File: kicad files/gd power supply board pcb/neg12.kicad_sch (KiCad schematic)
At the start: 22 parts, among them U1 MAX17580

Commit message: before erc
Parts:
- added H1, H2, H3, H4: MountingHole, MountingHole:MountingHole_2.2mm_M2, symbol Mechanical:MountingHole
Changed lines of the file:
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@@
     (effects (font (size 1.27 1.27)) (justify right))
+  )
+  (symbol (lib_id "Mechanical:MountingHole") (at 195.58 50.8 0) (unit 1)
+    (in_bom yes) (on_board yes) (fields_autoplaced)
+    (property "Reference" "H1" (id 0) (at 198.12 49.5299 0)
+      (effects (font (size 1.27 1.27)) (justify left))
+    )
+    (property "Value" "MountingHole" (id 1) (at 198.12 52.0699 0)
+      (effects (font (size 1.27 1.27)) (justify left))
+    )
+    (property "Footprint" "MountingHole:MountingHole_2.2mm_M2" (id 2) (at 195.58 50.8 0)
+      (effects (font (size 1.27 1.27)) hide)
+    )
+    (property "Datasheet" "~" (id 3) (at 195.58 50.8 0)
+      (effects (font (size 1.27 1.27)) hide)
+    )
   )
   (symbol (lib_id "My Library:TestPoint_Harwin") (at 146.05 74.93 0) (unit 1)
@@
     (pin "2")
   )
+  (symbol (lib_id "Mechanical:MountingHole") (at 195.58 57.15 0) (unit 1)
+    (in_bom yes) (on_board yes) (fields_autoplaced)
+    (property "Reference" "H2" (id 0) (at 198.12 55.8799 0)
+      (effects (font (size 1.27 1.27)) (justify left))
+    )
+    (property "Value" "MountingHole" (id 1) (at 198.12 58.4199 0)
+      (effects (font (size 1.27 1.27)) (justify left))
+    )
+    (property "Footprint" "MountingHole:MountingHole_2.2mm_M2" (id 2) (at 195.58 57.15 0)
+      (effects (font (size 1.27 1.27)) hide)
+    )
+    (property "Datasheet" "~" (id 3) (at 195.58 57.15 0)
+      (effects (font (size 1.27 1.27)) hide)
+    )
+  )
   (symbol (lib_id "power:GND") (at 198.12 88.9 0) (unit 1)
     (in_bom yes) (on_board yes) (fields_autoplaced)
@@
     (pin "2")
   )
+  (symbol (lib_id "Mechanical:MountingHole") (at 204.47 57.15 0) (unit 1)
+    (in_bom yes) (on_board yes) (fields_autoplaced)
+    (property "Reference" "H4" (id 0) (at 207.01 55.8799 0)
+      (effects (font (size 1.27 1.27)) (justify left))
+    )
+    (property "Value" "MountingHole" (id 1) (at 207.01 58.4199 0)
+      (effects (font (size 1.27 1.27)) (justify left))
+    )
+    (property "Footprint" "MountingHole:MountingHole_2.2mm_M2" (id 2) (at 204.47 57.15 0)
+      (effects (font (size 1.27 1.27)) hide)
+    )
+    (property "Datasheet" "~" (id 3) (at 204.47 57.15 0)
+      (effects (font (size 1.27 1.27)) hide)
+    )
+  )
   (symbol (lib_id "My Library:TestPoint_Harwin") (at 102.87 74.93 0) (unit 1)
     (in_bom yes) (on_board yes)
@@
     (pin "1")
   )
+  (symbol (lib_id "Mechanical:MountingHole") (at 204.47 50.8 0) (unit 1)
+    (in_bom yes) (on_board yes) (fields_autoplaced)
+    (property "Reference" "H3" (id 0) (at 207.01 49.5299 0)
+      (effects (font (size 1.27 1.27)) (justify left))
+    )
+    (property "Value" "MountingHole" (id 1) (at 207.01 52.0699 0)
+      (effects (font (size 1.27 1.27)) (justify left))
+    )
+    (property "Footprint" "MountingHole:MountingHole_2.2mm_M2" (id 2) (at 204.47 50.8 0)
+      (effects (font (size 1.27 1.27)) hide)
+    )
+    (property "Datasheet" "~" (id 3) (at 204.47 50.8 0)
+      (effects (font (size 1.27 1.27)) hide)
+    )
+  )
   (symbol (lib_id "My Library:R_0805") (at 151.13 74.93 90) (unit 1)

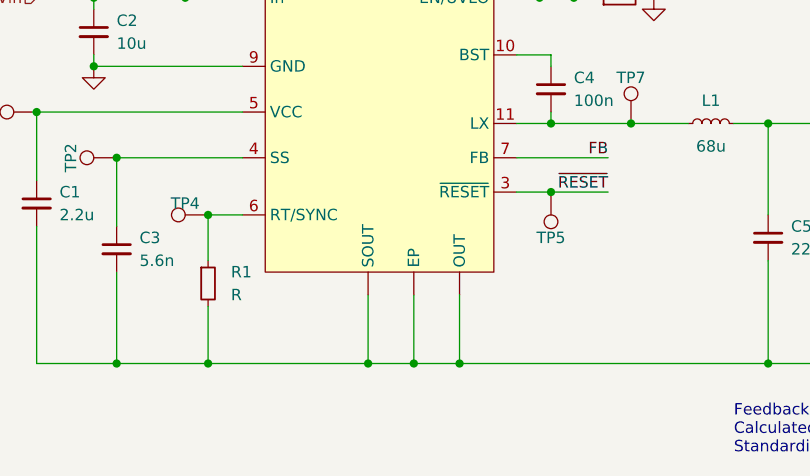
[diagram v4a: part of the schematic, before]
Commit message: initial floor planning done
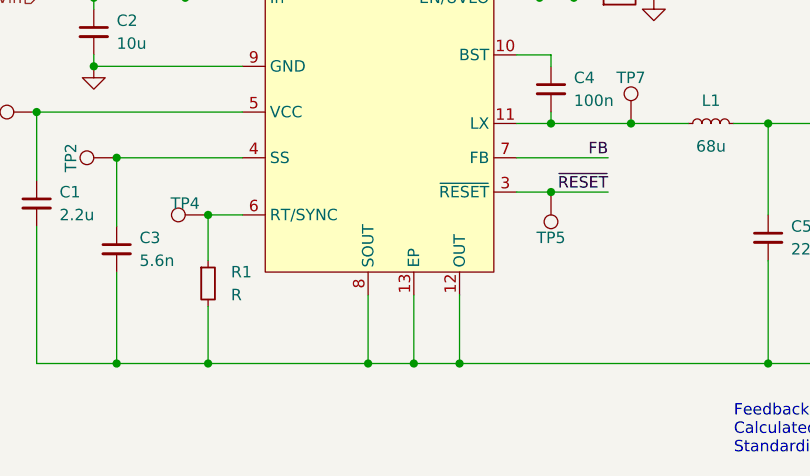
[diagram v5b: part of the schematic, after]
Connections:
- net Neg12_Out: now also U1.12 (OUT), U1.13 (EP), U1.8 (SOUT); no longer U1. (SOUT)
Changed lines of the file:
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@@
   (junction (at 102.87 74.93) (diameter 0) (color 0 0 0 0)
   )
+  (junction (at 105.41 115.57) (diameter 0) (color 0 0 0 0)
+  )
+  (junction (at 128.27 115.57) (diameter 0) (color 0 0 0 0)
+  )
+  (junction (at 86.36 87.63) (diameter 0) (color 0 0 0 0)
+  )
+  (junction (at 95.25 92.71) (diameter 0) (color 0 0 0 0)
+  )
+  (junction (at 179.07 115.57) (diameter 0) (color 0 0 0 0)
+  )
+  (junction (at 179.07 88.9) (diameter 0) (color 0 0 0 0)
+  )
+  (junction (at 143.51 88.9) (diameter 0) (color 0 0 0 0)
+  )
+  (junction (at 189.23 115.57) (diameter 0) (color 0 0 0 0)
+  )
+  (junction (at 167.64 88.9) (diameter 0) (color 0 0 0 0)
+  )
   (junction (at 123.19 115.57) (diameter 0) (color 0 0 0 0)
   )
-  (junction (at 105.41 115.57) (diameter 0) (color 0 0 0 0)
-  )
-  (junction (at 128.27 115.57) (diameter 0) (color 0 0 0 0)
-  )
-  (junction (at 86.36 87.63) (diameter 0) (color 0 0 0 0)
-  )
-  (junction (at 95.25 92.71) (diameter 0) (color 0 0 0 0)
-  )
-  (junction (at 179.07 115.57) (diameter 0) (color 0 0 0 0)
-  )
-  (junction (at 179.07 88.9) (diameter 0) (color 0 0 0 0)
-  )
-  (junction (at 143.51 88.9) (diameter 0) (color 0 0 0 0)
-  )
-  (junction (at 189.23 115.57) (diameter 0) (color 0 0 0 0)
-  )
-  (junction (at 167.64 88.9) (diameter 0) (color 0 0 0 0)
-  )
   (junction (at 143.51 96.52) (diameter 0) (color 0 0 0 0)
   )
@@
     (stroke (width 0) (type default) (color 0 0 0 0))
   )
+  (wire (pts (xy 123.19 107.95) (xy 123.19 115.57))
+    (stroke (width 0) (type default) (color 0 0 0 0))
+  )
   (wire (pts (xy 92.71 74.93) (xy 86.36 74.93))
     (stroke (width 0) (type default) (color 0 0 0 0))
@@
     (stroke (width 0) (type default) (color 0 0 0 0))
   )
+  (wire (pts (xy 123.19 115.57) (xy 128.27 115.57))
+    (stroke (width 0) (type default) (color 0 0 0 0))
+  )
   (wire (pts (xy 95.25 115.57) (xy 105.41 115.57))
     (stroke (width 0) (type default) (color 0 0 0 0))
@@
     (stroke (width 0) (type default) (color 0 0 0 0))
   )
-  (wire (pts (xy 123.19 115.57) (xy 128.27 115.57))
-    (stroke (width 0) (type default) (color 0 0 0 0))
-  )
   (wire (pts (xy 86.36 100.33) (xy 86.36 115.57))
-    (stroke (width 0) (type default) (color 0 0 0 0))
-  )
-  (wire (pts (xy 123.19 107.95) (xy 123.19 115.57))
     (stroke (width 0) (type default) (color 0 0 0 0))
   )
@@
       (effects (font (size 1.27 1.27)) hide)
     )
-    (pin "")
-    (pin "")
-    (pin "")
+    (pin "13")
+    (pin "12")
+    (pin "8")
     (pin "1")
     (pin "10")

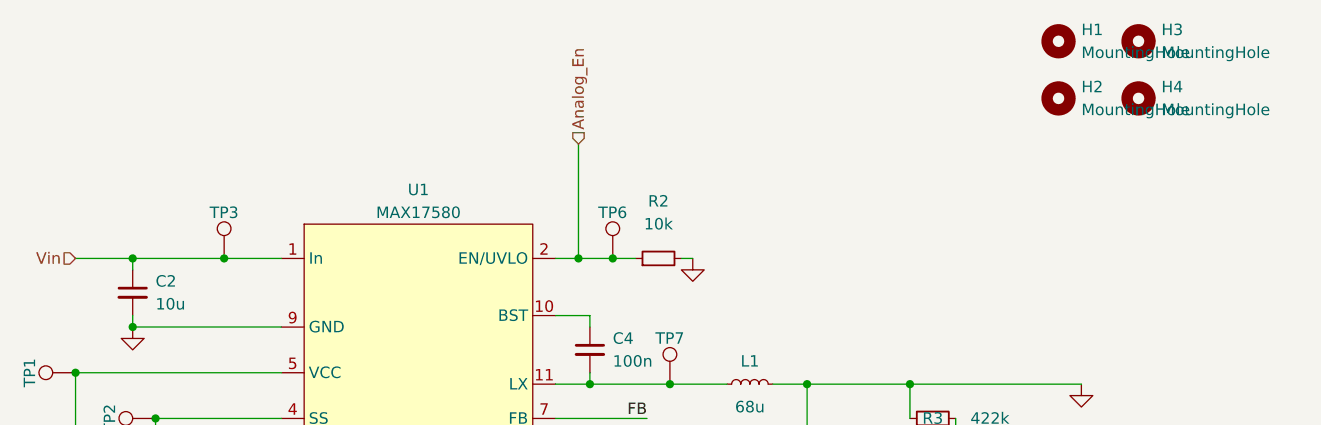
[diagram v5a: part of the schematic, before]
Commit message: minor fixes and compacting the floorplan. stacked 5V supplies for maximum minimage.
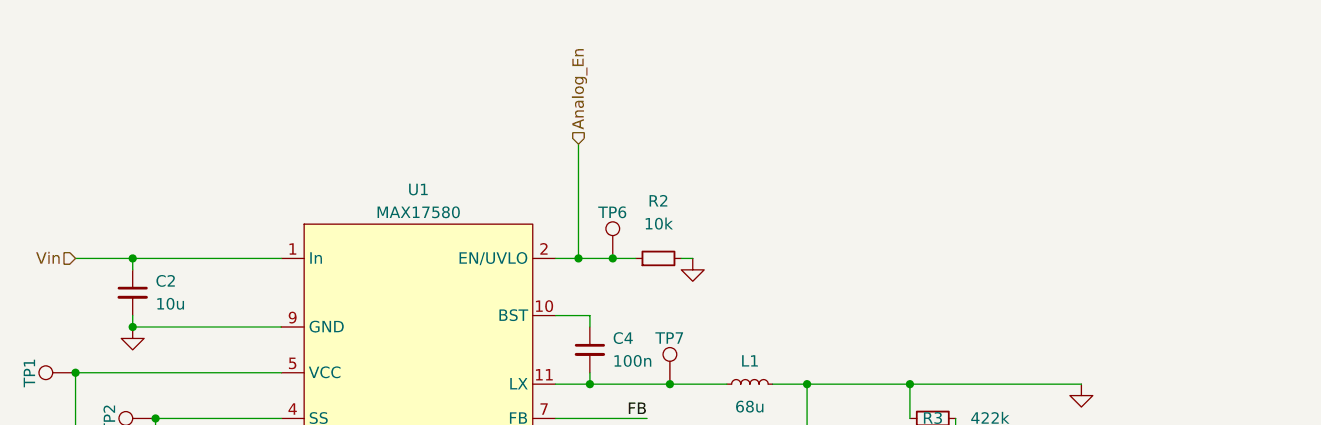
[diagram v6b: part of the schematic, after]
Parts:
- removed H1, H2, H3, H4: MountingHole, MountingHole:MountingHole_2.2mm_M2, symbol Mechanical:MountingHole
- removed TP3: TestPoint_Harwin, My Libraries:Harwin-S1751-46-Test-Point, symbol My Library:TestPoint_Harwin
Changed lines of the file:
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@@
   (junction (at 92.71 74.93) (diameter 0) (color 0 0 0 0)
   )
-  (junction (at 102.87 74.93) (diameter 0) (color 0 0 0 0)
-  )
   (junction (at 105.41 115.57) (diameter 0) (color 0 0 0 0)
   )
@@
     (stroke (width 0) (type default) (color 0 0 0 0))
   )
-  (wire (pts (xy 102.87 74.93) (xy 109.22 74.93))
-    (stroke (width 0) (type default) (color 0 0 0 0))
-  )
-  (wire (pts (xy 92.71 74.93) (xy 102.87 74.93))
+  (wire (pts (xy 92.71 74.93) (xy 109.22 74.93))
     (stroke (width 0) (type default) (color 0 0 0 0))
   )
@@
     (effects (font (size 1.27 1.27)) (justify right))
   )
-  (symbol (lib_id "Mechanical:MountingHole") (at 195.58 50.8 0) (unit 1)
-    (in_bom yes) (on_board yes) (fields_autoplaced)
-    (property "Reference" "H1" (id 0) (at 198.12 49.5299 0)
-      (effects (font (size 1.27 1.27)) (justify left))
-    )
-    (property "Value" "MountingHole" (id 1) (at 198.12 52.0699 0)
-      (effects (font (size 1.27 1.27)) (justify left))
-    )
-    (property "Footprint" "MountingHole:MountingHole_2.2mm_M2" (id 2) (at 195.58 50.8 0)
-      (effects (font (size 1.27 1.27)) hide)
-    )
-    (property "Datasheet" "~" (id 3) (at 195.58 50.8 0)
-      (effects (font (size 1.27 1.27)) hide)
-    )
-  )
   (symbol (lib_id "My Library:TestPoint_Harwin") (at 146.05 74.93 0) (unit 1)
     (in_bom yes) (on_board yes)
@@
     (pin "2")
   )
-  (symbol (lib_id "Mechanical:MountingHole") (at 195.58 57.15 0) (unit 1)
-    (in_bom yes) (on_board yes) (fields_autoplaced)
-    (property "Reference" "H2" (id 0) (at 198.12 55.8799 0)
-      (effects (font (size 1.27 1.27)) (justify left))
-    )
-    (property "Value" "MountingHole" (id 1) (at 198.12 58.4199 0)
-      (effects (font (size 1.27 1.27)) (justify left))
-    )
-    (property "Footprint" "MountingHole:MountingHole_2.2mm_M2" (id 2) (at 195.58 57.15 0)
-      (effects (font (size 1.27 1.27)) hide)
-    )
-    (property "Datasheet" "~" (id 3) (at 195.58 57.15 0)
-      (effects (font (size 1.27 1.27)) hide)
-    )
-  )
   (symbol (lib_id "power:GND") (at 198.12 88.9 0) (unit 1)
     (in_bom yes) (on_board yes) (fields_autoplaced)
@@
     (pin "2")
   )
-  (symbol (lib_id "Mechanical:MountingHole") (at 204.47 57.15 0) (unit 1)
-    (in_bom yes) (on_board yes) (fields_autoplaced)
-    (property "Reference" "H4" (id 0) (at 207.01 55.8799 0)
-      (effects (font (size 1.27 1.27)) (justify left))
-    )
-    (property "Value" "MountingHole" (id 1) (at 207.01 58.4199 0)
-      (effects (font (size 1.27 1.27)) (justify left))
-    )
-    (property "Footprint" "MountingHole:MountingHole_2.2mm_M2" (id 2) (at 204.47 57.15 0)
-      (effects (font (size 1.27 1.27)) hide)
-    )
-    (property "Datasheet" "~" (id 3) (at 204.47 57.15 0)
-      (effects (font (size 1.27 1.27)) hide)
-    )
-  )
-  (symbol (lib_id "My Library:TestPoint_Harwin") (at 102.87 74.93 0) (unit 1)
-    (in_bom yes) (on_board yes)
-    (property "Reference" "TP3" (id 0) (at 102.87 69.85 0))
-    (property "Value" "TestPoint_Harwin" (id 1) (at 102.87 69.85 0)
-      (effects (font (size 1.27 1.27)) hide)
-    )
-    (property "Footprint" "My Libraries:Harwin-S1751-46-Test-Point" (id 2) (at 107.95 74.93 0)
-      (effects (font (size 1.27 1.27)) hide)
-    )
-    (property "Datasheet" "~" (id 3) (at 107.95 74.93 0)
-      (effects (font (size 1.27 1.27)) hide)
-    )
-    (pin "1")
-  )
   (symbol (lib_id "My Library:C_0805") (at 86.36 97.79 0) (unit 1)
     (in_bom yes) (on_board yes) (fields_autoplaced)
@@
     )
     (pin "1")
-  )
-  (symbol (lib_id "Mechanical:MountingHole") (at 204.47 50.8 0) (unit 1)
-    (in_bom yes) (on_board yes) (fields_autoplaced)
-    (property "Reference" "H3" (id 0) (at 207.01 49.5299 0)
-      (effects (font (size 1.27 1.27)) (justify left))
-    )
-    (property "Value" "MountingHole" (id 1) (at 207.01 52.0699 0)
-      (effects (font (size 1.27 1.27)) (justify left))
-    )
-    (property "Footprint" "MountingHole:MountingHole_2.2mm_M2" (id 2) (at 204.47 50.8 0)
-      (effects (font (size 1.27 1.27)) hide)
-    )
-    (property "Datasheet" "~" (id 3) (at 204.47 50.8 0)
-      (effects (font (size 1.27 1.27)) hide)
-    )
   )
   (symbol (lib_id "My Library:R_0805") (at 151.13 74.93 90) (unit 1)
@@
       (effects (font (size 1.27 1.27)) hide)
     )
-    (pin "13")
-    (pin "12")
-    (pin "8")
     (pin "1")
     (pin "10")
     (pin "11")
+    (pin "12")
+    (pin "13")
     (pin "2")
     (pin "3")
@@
     (pin "6")
     (pin "7")
+    (pin "8")
     (pin "9")
   )
